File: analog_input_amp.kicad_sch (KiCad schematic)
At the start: 41 parts

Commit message: Update: slowly drawing schematic
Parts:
- removed C?: 100n, symbol Device:C
- removed C?: 1u, symbol Device:C
- removed D? (x4): BAT54, symbol Device:D_Schottky
- removed D? (x2): 1N4148, symbol Device:D
- removed R?: 50, symbol Device:R
- removed R? (x2): 0, symbol Device:R
- removed R?: 10k, symbol Device:R
- added C502: 10u, symbol Device:C
- added C509: 100n, symbol Device:C
- added D501: SD12C, symbol Device:D_TVS
- added D502, D503: BAT54, symbol Device:D_Schottky
- added R502: 0, symbol Device:R
- added R506: 62, symbol Device:R
- added R507, R509: 200, symbol Device:R
- added R508: 27, symbol Device:R
- C501, C507: renamed from C?; value C -> 3.3n
- C503, C505: renamed from C?; value C -> 8.2n
- C504: renamed from C?; value C -> 10n
- C508: renamed from C?; value 1u -> 100n
- C511, C512: renamed from C?; value 510p -> 1.5n
- C513, C514: renamed from C?; value 1n -> 1.5n
- L501, L504: renamed from L?; value L -> 18u
- L502, L503: renamed from L?; value L -> 33u
- R501, R505: renamed from R?; value R -> 49.9
- R503, R504: renamed from R?; value R -> 3.3k
- R510, R511: renamed from R?; value 100 -> 24
- R512, R513: renamed from R?; value 100 -> 220
- gave numbers to parts that had none: 7
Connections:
- net +3V3A: now also R502.2; no longer U501.3 (VS+)
- net GNDA: now also C502.2, C509.1, D501.1 (A1), D503.2 (A), R506.1
- net IN: now also D501.2 (A2)
- net OUT+: now also C514.1, R515.2, TP502.1
- net OUT-: now also C513.1, R514.2, TP501.1
- net at C507.1, C508.1, L504.2: now also R506.2
- net at C510.2, R510.1, R512.1: now also D502.2 (A), D503.1 (K), R507.2; no longer C508.2
- net at C510.1, R511.1, R513.1: now also R509.2
- new net: C508.2, R507.1
- new net: C509.2, R508.1
- new net: R508.2, R509.1
- new net VS+: C502.1, D502.1 (K), R502.1, U501.3 (VS+)
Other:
- moved on the sheet: C501, C503, C504, C505, C506, C507, C508, C510, C511, C512, C513, C514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

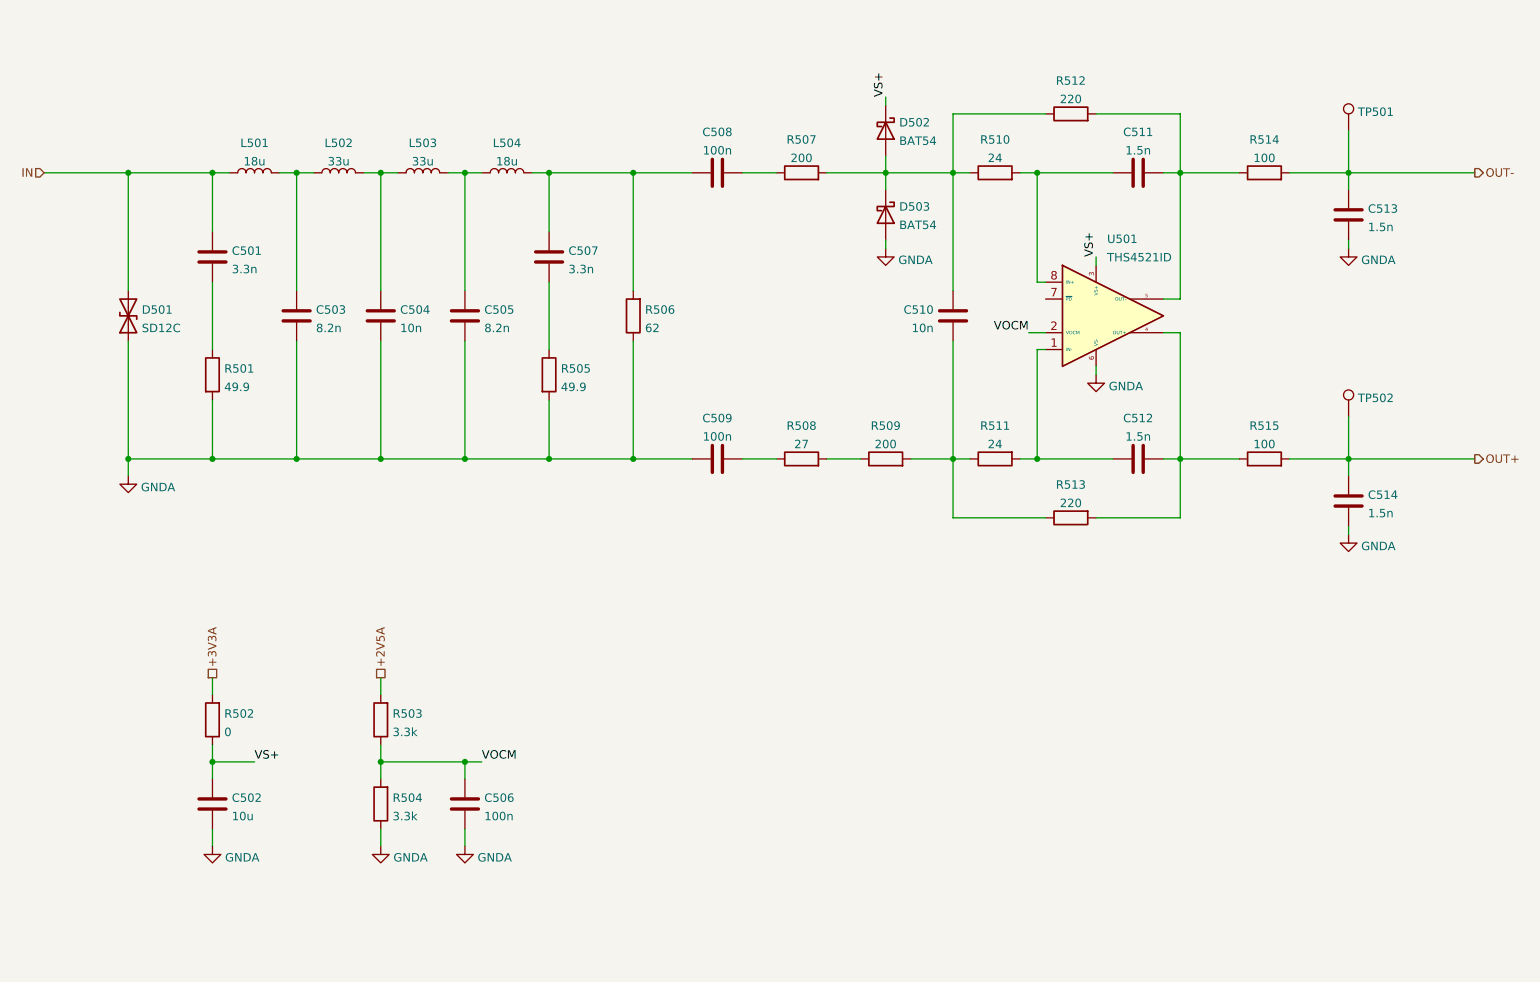
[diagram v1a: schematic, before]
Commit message: Schematic: added VCTCXO, clk out, ref in, separated power supply into a new sheet
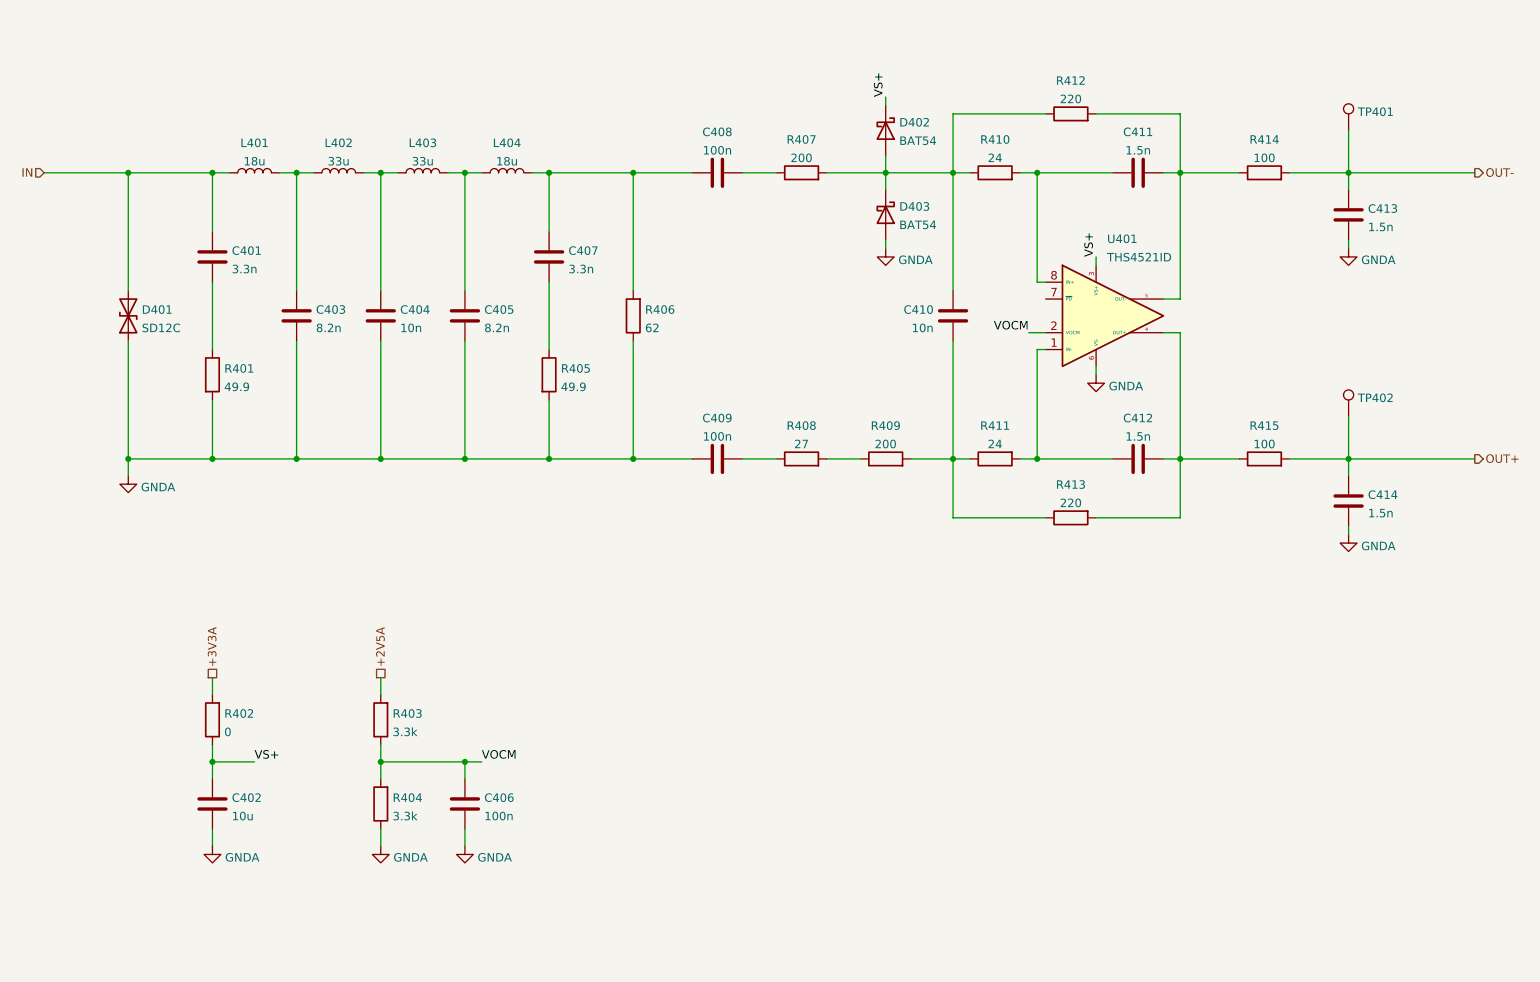
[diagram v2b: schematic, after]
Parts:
- renumbered C501 to C401, C502 to C402, C503 to C403, C504 to C404, C505 to C405, C506 to C406, C507 to C407, C508 to C408, C509 to C409, C510 to C410, C511 to C411, C512 to C412, C513 to C413, C514 to C414, D501 to D401, D502 to D402, D503 to D403, L501 to L401, L502 to L402, L503 to L403, L504 to L404, R501 to R401, R502 to R402, R503 to R403, R504 to R404, R505 to R405, R506 to R406, R507 to R407, R508 to R408, R509 to R409, R510 to R410, R511 to R411, R512 to R412, R513 to R413, R514 to R414, R515 to R415, TP501 to TP401, TP502 to TP402, U501 to U401

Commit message: Schematic updated
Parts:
- C501: renamed from C401; footprint (none) -> Capacitor_SMD:C_0805_2012Metric
- C503: renamed from C403; footprint (none) -> Capacitor_SMD:C_0805_2012Metric
- C504: renamed from C404; footprint (none) -> Capacitor_SMD:C_0805_2012Metric
- C505: renamed from C405; footprint (none) -> Capacitor_SMD:C_0805_2012Metric
- C506: renamed from C406; footprint (none) -> Capacitor_SMD:C_0805_2012Metric
- C507: renamed from C407; footprint (none) -> Capacitor_SMD:C_0805_2012Metric
- C508: renamed from C408; footprint (none) -> Capacitor_SMD:C_0805_2012Metric
- C509: renamed from C409; footprint (none) -> Capacitor_SMD:C_0805_2012Metric
- C510: renamed from C410; footprint (none) -> Capacitor_SMD:C_0805_2012Metric
- C511: renamed from C411; footprint (none) -> Capacitor_SMD:C_0805_2012Metric
- C512: renamed from C412; footprint (none) -> Capacitor_SMD:C_0805_2012Metric
- C513: renamed from C413; footprint (none) -> Capacitor_SMD:C_0805_2012Metric
- C514: renamed from C414; footprint (none) -> Capacitor_SMD:C_0805_2012Metric
- R501: renamed from R401; footprint (none) -> Resistor_SMD:R_0805_2012Metric
- R502: renamed from R402; footprint (none) -> Resistor_SMD:R_0805_2012Metric
- R503: renamed from R403; footprint (none) -> Resistor_SMD:R_0805_2012Metric
- R504: renamed from R404; footprint (none) -> Resistor_SMD:R_0805_2012Metric
- R505: renamed from R405; footprint (none) -> Resistor_SMD:R_0805_2012Metric
- R506: renamed from R406; footprint (none) -> Resistor_SMD:R_0805_2012Metric
- R507: renamed from R407; footprint (none) -> Resistor_SMD:R_0805_2012Metric
- R508: renamed from R408; footprint (none) -> Resistor_SMD:R_0805_2012Metric
- R509: renamed from R409; footprint (none) -> Resistor_SMD:R_0805_2012Metric
- R510: renamed from R410; footprint (none) -> Resistor_SMD:R_0805_2012Metric
- R511: renamed from R411; footprint (none) -> Resistor_SMD:R_0805_2012Metric
- R512: renamed from R412; footprint (none) -> Resistor_SMD:R_0805_2012Metric
- R513: renamed from R413; footprint (none) -> Resistor_SMD:R_0805_2012Metric
- R514: renamed from R414; footprint (none) -> Resistor_SMD:R_0805_2012Metric
- R515: renamed from R415; footprint (none) -> Resistor_SMD:R_0805_2012Metric
- TP501: renamed from TP401; footprint (none) -> TestPoint:TestPoint_THTPad_D1.0mm_Drill0.5mm
- TP502: renamed from TP402; footprint (none) -> TestPoint:TestPoint_THTPad_D1.0mm_Drill0.5mm
- renumbered C402 to C502, D401 to D501, D402 to D502, D403 to D503, L401 to L501, L402 to L502, L403 to L503, L404 to L504, U401 to U501
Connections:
- net GNDA: no longer C503.2, C504.2, C505.2, C509.1, C513.2, C514.2, D501.1 (A1), D503.2 (A), R501.2, R505.2, R506.1, U501.6 (VS-)
- net +2V5A renamed +2.5VA
- net +3V3A renamed +3.3VA
- new net GND: C503.2, C504.2, C505.2, C509.1, C513.2, C514.2, D501.1 (A1), D503.2 (A), R501.2, R505.2, R506.1, U501.6 (VS-)

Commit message: Schematic sketching done
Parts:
- removed C514: 1.5n, Capacitor_SMD:C_0805_2012Metric, symbol Device:C
- removed D502, D503: BAT54, symbol Device:D_Schottky
- added C?: 1.5n, Capacitor_SMD:C_0805_2012Metric, symbol Device:C
- added D? (x2): BAT54J, Diode_SMD:D_SOD-323F, symbol Diode:BAT54J
- C501, C503, C504, C505, C507: Spec1 (none) -> 25V; Spec2 (none) -> C0G; Tolerance (none) -> 5%
- C508: Spec1 (none) -> 25V; Spec2 (none) -> U2J; Tolerance (none) -> 10%
- C509: Spec1 (none) -> 10V; Spec2 (none) -> U2J; Tolerance (none) -> 10%
- C510: Spec1 (none) -> 50V; Spec2 (none) -> C0G; Tolerance (none) -> 5%
- C511, C512, C513: Spec1 (none) -> 10V; Spec2 (none) -> C0G; Tolerance (none) -> 5%
- L501, L502, L503, L504, R501, R503, R504, R505, R506, R507, R508, R509, R510, R511, R512, R513, R514, R515: Tolerance (none) -> 5%
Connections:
- net GNDA is gone; now on net GND: C502.2, C506.2, R504.1
- net GND: now also C?.2, D?.2 (A)
- net OUT+: now also C?.1
- net VS+: now also D?.1 (K)
- net at C510.2, R507.2, R510.1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: now also D?.1 (K), D?.2 (A)
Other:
- moved on the sheet: C510, C513, R512, R513, TP501, TP502

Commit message: Update schematic layout, separate into sheets
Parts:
- C310: renamed from C510; Spec1 50V -> 10V
- gave numbers to parts that had none: 3
- renumbered C501 to C301, C502 to C302, C503 to C303, C504 to C304, C505 to C305, C506 to C306, C507 to C307, C508 to C308, C509 to C309, C511 to C311, C512 to C312, C513 to C313, D501 to D301, L501 to L301, L502 to L302, L503 to L303, L504 to L304, R501 to R301, R502 to R302, R503 to R303, R504 to R304, R505 to R305, R506 to R306, R507 to R307, R508 to R308, R509 to R309, R510 to R310, R511 to R311, R512 to R312, R513 to R313, R514 to R314, R515 to R315, TP501 to TP301, TP502 to TP302, U501 to U301

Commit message: Schematic update
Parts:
- C302: value 10u -> 4.7u; footprint (none) -> Capacitor_SMD:C_0805_2012Metric; Spec1 (none) -> 16V; Spec2 (none) -> X5R; Tolerance (none) -> 20%
- C306: Spec1 (none) -> 16V; Spec2 (none) -> X5R; Tolerance (none) -> 20%
- C308: footprint Capacitor_SMD:C_0805_2012Metric -> Capacitor_SMD:C_1206_3216Metric
- C309: footprint Capacitor_SMD:C_0805_2012Metric -> Capacitor_SMD:C_1206_3216Metric; Spec1 10V -> 16V
- C310, C311, C312, C313, C314: Spec1 10V -> 16V
- R303, R304: value 3.3k -> 1k
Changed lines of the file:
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@@
     (property "Reference" "C308" (id 0) (at 139.7 36.3491 90))
     (property "Value" "100n" (id 1) (at 139.7 39.1242 90))
-    (property "Footprint" "Capacitor_SMD:C_0805_2012Metric" (id 2) (at 143.51 49.8348 0)
+    (property "Footprint" "Capacitor_SMD:C_1206_3216Metric" (id 2) (at 143.51 49.8348 0)
       (effects (font (size 1.27 1.27)) hide)
     )
@@
       (effects (font (size 1.27 1.27)) hide)
     )
-    (property "Spec1" "10V" (id 4) (at 203.2 103.8387 90))
+    (property "Spec1" "16V" (id 4) (at 203.2 103.8387 90))
     (property "Spec2" "C0G" (id 5) (at 203.2 106.6138 90))
     (property "Tolerance" "5%" (id 6) (at 203.2 109.3889 90))
@@
       (effects (font (size 1.27 1.27)) hide)
     )
-    (property "Spec1" "10V" (id 4) (at 174.371 72.869 0)
+    (property "Spec1" "16V" (id 4) (at 174.371 72.869 0)
       (effects (font (size 1.27 1.27)) (justify right))
     )
@@
       (effects (font (size 1.27 1.27)) (justify right))
     )
-    (property "Value" "3.3k" (id 1) (at 90.678 147.9166 0)
+    (property "Value" "1k" (id 1) (at 90.678 147.9166 0)
       (effects (font (size 1.27 1.27)) (justify right))
     )
@@
     )
     (property "Datasheet" "~" (id 3) (at 101.6 146.05 0)
+      (effects (font (size 1.27 1.27)) hide)
+    )
+    (property "Spec1" "16V" (id 4) (at 101.6 146.05 0)
+      (effects (font (size 1.27 1.27)) hide)
+    )
+    (property "Spec2" "X5R" (id 5) (at 101.6 146.05 0)
+      (effects (font (size 1.27 1.27)) hide)
+    )
+    (property "Tolerance" "20%" (id 6) (at 101.6 146.05 0)
       (effects (font (size 1.27 1.27)) hide)
     )
@@
     (property "Reference" "C309" (id 0) (at 139.7 79.5291 90))
     (property "Value" "100n" (id 1) (at 139.7 82.3042 90))
-    (property "Footprint" "Capacitor_SMD:C_0805_2012Metric" (id 2) (at 143.51 93.0148 0)
+    (property "Footprint" "Capacitor_SMD:C_1206_3216Metric" (id 2) (at 143.51 93.0148 0)
       (effects (font (size 1.27 1.27)) hide)
     )
@@
       (effects (font (size 1.27 1.27)) hide)
     )
-    (property "Spec1" "10V" (id 4) (at 139.7 85.0793 90))
+    (property "Spec1" "16V" (id 4) (at 139.7 85.0793 90))
     (property "Spec2" "U2J" (id 5) (at 139.7 87.8544 90))
     (property "Tolerance" "10%" (id 6) (at 139.7 90.6295 90))
@@
       (effects (font (size 1.27 1.27)) hide)
     )
-    (property "Spec1" "10V" (id 4) (at 203.2 41.8993 90))
+    (property "Spec1" "16V" (id 4) (at 203.2 41.8993 90))
     (property "Spec2" "C0G" (id 5) (at 203.2 44.6744 90))
     (property "Tolerance" "5%" (id 6) (at 203.2 47.4495 90))
@@
       (effects (font (size 1.27 1.27)) (justify left))
     )
-    (property "Value" "10u" (id 1) (at 66.421 147.9166 0)
-      (effects (font (size 1.27 1.27)) (justify left))
-    )
-    (property "Footprint" "" (id 2) (at 64.4652 149.86 0)
+    (property "Value" "4.7u" (id 1) (at 66.421 147.9166 0)
+      (effects (font (size 1.27 1.27)) (justify left))
+    )
+    (property "Footprint" "Capacitor_SMD:C_0805_2012Metric" (id 2) (at 64.4652 149.86 0)
       (effects (font (size 1.27 1.27)) hide)
     )
     (property "Datasheet" "~" (id 3) (at 63.5 146.05 0)
+      (effects (font (size 1.27 1.27)) hide)
+    )
+    (property "Spec1" "16V" (id 4) (at 63.5 146.05 0)
+      (effects (font (size 1.27 1.27)) hide)
+    )
+    (property "Spec2" "X5R" (id 5) (at 63.5 146.05 0)
+      (effects (font (size 1.27 1.27)) hide)
+    )
+    (property "Tolerance" "20%" (id 6) (at 63.5 146.05 0)
       (effects (font (size 1.27 1.27)) hide)
     )
@@
       (effects (font (size 1.27 1.27)) hide)
     )
-    (property "Spec1" "10V" (id 4) (at 237.871 58.899 0)
+    (property "Spec1" "16V" (id 4) (at 237.871 58.899 0)
       (effects (font (size 1.27 1.27)) (justify left))
     )
@@
       (effects (font (size 1.27 1.27)) (justify right))
     )
-    (property "Value" "3.3k" (id 1) (at 90.678 135.2166 0)
+    (property "Value" "1k" (id 1) (at 90.678 135.2166 0)
       (effects (font (size 1.27 1.27)) (justify right))
     )
@@
       (effects (font (size 1.27 1.27)) hide)
     )
-    (property "Spec1" "10V" (id 4) (at 237.871 102.079 0)
-      (effects (font (size 1.27 1.27)) (justify left))
-    )
+    (property "Spec1" "16V" (id 4) (at 237.871 102.079 0)
+      (effects (font (size 1.27 1.27)) (justify left))
+    )
